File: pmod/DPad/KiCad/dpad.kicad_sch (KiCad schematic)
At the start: 13 parts, among them SW1 SW_Push, SW2 SW_Push, SW3 SW_Push, SW4 SW_Push

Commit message: Fixed resistor labels to correct format (10K).
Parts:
- R1, R2, R3, R4: value 10 k -> 10K
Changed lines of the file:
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@@
 			)
 		)
-		(property "Value" "10 k"
+		(property "Value" "10K"
 			(at 109.22 91.4399 0)
 			(effects
@@
 			)
 		)
-		(property "Value" "10 k"
+		(property "Value" "10K"
 			(at 81.28 91.4399 0)
 			(effects
@@
 			)
 		)
-		(property "Value" "10 k"
+		(property "Value" "10K"
 			(at 95.25 91.4399 0)
 			(effects
@@
 			)
 		)
-		(property "Value" "10 k"
+		(property "Value" "10K"
 			(at 123.19 91.4399 0)
 			(effects

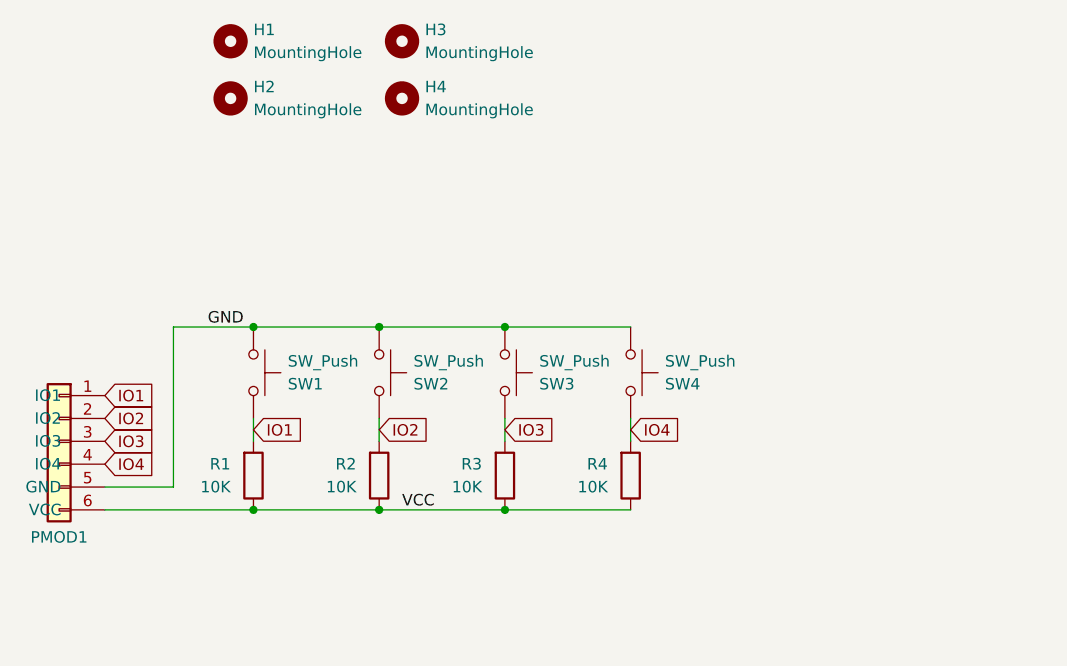
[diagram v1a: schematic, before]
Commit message: Added debounce capacitors. Added drill holes for switches.
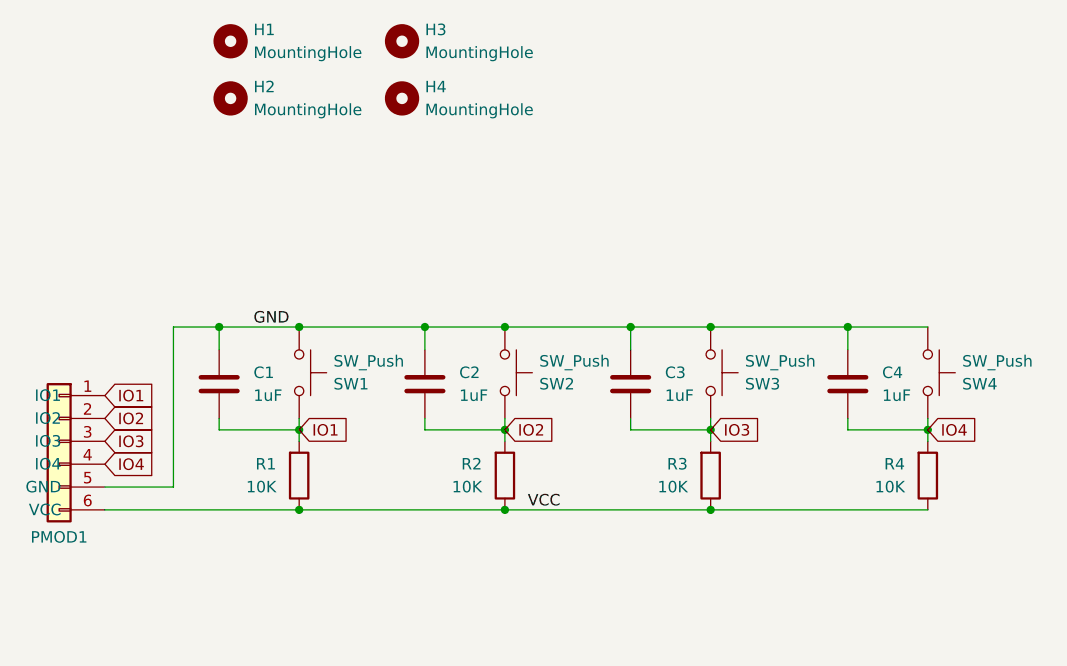
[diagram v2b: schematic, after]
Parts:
- added C1, C2, C3, C4: 1uF, Custom:C_Disc_D6.0mm_W4mm_P5.00mm, symbol Device:C
- SW1, SW2, SW3, SW4: footprint Button_Switch_THT:SW_PUSH-12mm_Wuerth-430476085716 -> Custom:SW_PUSH-12mm
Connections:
- net GND: now also C1.1, C2.1, C3.1, C4.1
- net IO1: now also C1.2
- net IO2: now also C2.2
- net IO3: now also C3.2
- net IO4: now also C4.2
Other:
- moved on the sheet: R1, R2, R3, R4, SW1, SW2, SW3, SW4

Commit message: Increased track width. Rounded edges of board. Fixed right angle connector.
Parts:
- PMOD1: footprint Connector_PinHeader_2.54mm:PinHeader_1x06_P2.54mm_Vertical -> Connector_PinHeader_2.54mm:PinHeader_1x06_P2.54mm_Horizontal
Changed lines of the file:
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@@
 			)
 		)
-		(property "Footprint" "Connector_PinHeader_2.54mm:PinHeader_1x06_P2.54mm_Vertical"
+		(property "Footprint" "Connector_PinHeader_2.54mm:PinHeader_1x06_P2.54mm_Horizontal"
 			(at 62.23 86.36 0)
 			(effects

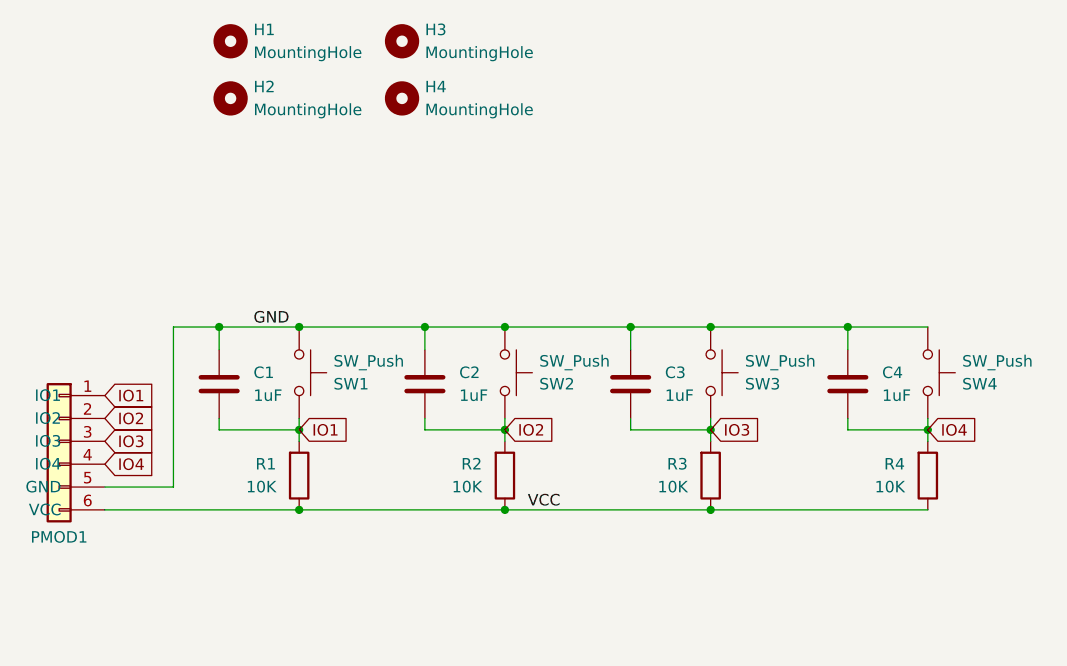
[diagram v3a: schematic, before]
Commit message: fix: prepare all board for manufacturing
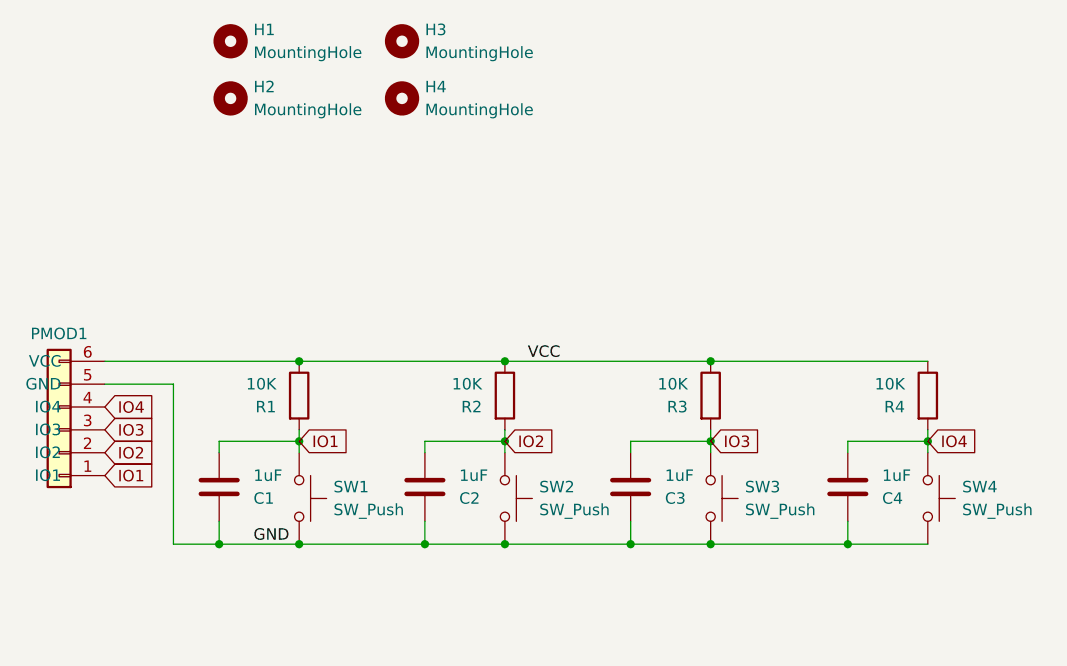
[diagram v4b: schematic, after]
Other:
- moved on the sheet: C1, C2, C3, C4, PMOD1, R1, R2, R3, R4, SW1, SW2, SW3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

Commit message: docs: add images, fix docs
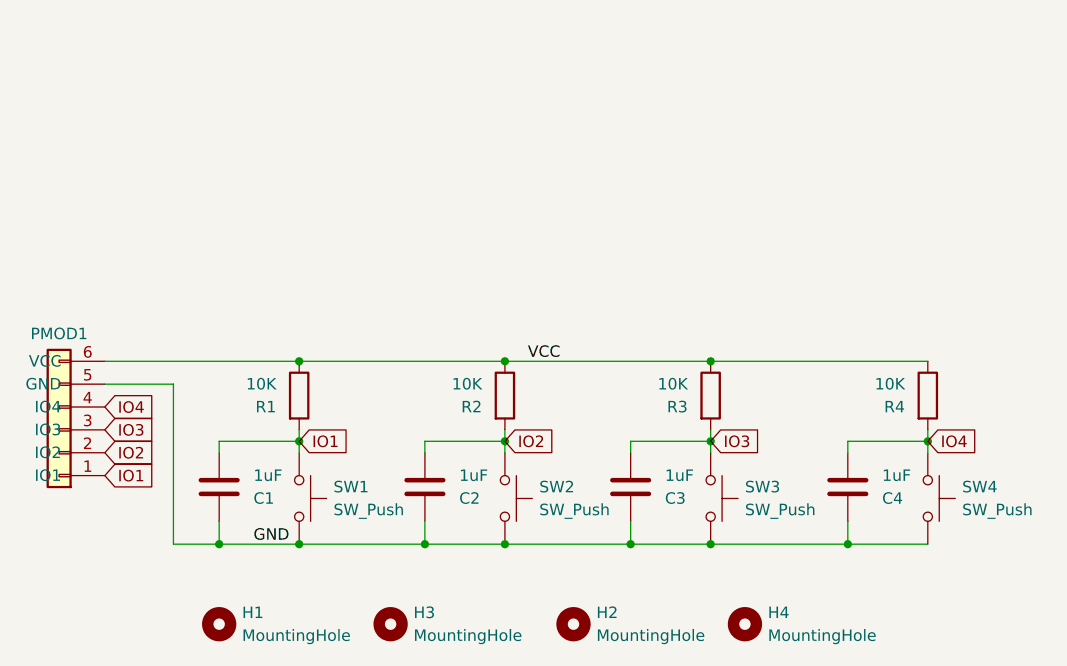
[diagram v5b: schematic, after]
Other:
- moved on the sheet: H1, H2, H3, H4
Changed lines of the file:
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@@
 	(symbol
 		(lib_id "Mechanical:MountingHole")
-		(at 81.28 48.26 0)
+		(at 119.38 106.68 0)
 		(unit 1)
 		(body_style 1)
@@
 		(fields_autoplaced yes)
 		(property "Reference" "H2"
-			(at 83.82 46.9899 0)
+			(at 121.92 105.4099 0)
 			(show_name no)
 			(do_not_autoplace no)
@@
 		)
 		(property "Value" "MountingHole"
-			(at 83.82 49.5299 0)
+			(at 121.92 107.9499 0)
 			(show_name no)
 			(do_not_autoplace no)
@@
 		)
 		(property "Footprint" "MountingHole:MountingHole_3.2mm_M3"
-			(at 81.28 48.26 0)
-			(hide yes)
-			(show_name no)
-			(do_not_autoplace no)
-			(effects
-				(font
-					(size 1.27 1.27)
-				)
-			)
-		)
-		(property "Datasheet" ""
-			(at 81.28 48.26 0)
+			(at 119.38 106.68 0)
+			(hide yes)
+			(show_name no)
+			(do_not_autoplace no)
+			(effects
+				(font
+					(size 1.27 1.27)
+				)
+			)
+		)
+		(property "Datasheet" ""
+			(at 119.38 106.68 0)
 			(hide yes)
 			(show_name no)
@@
 		)
 		(property "Description" "Mounting Hole without connection"
-			(at 81.28 48.26 0)
+			(at 119.38 106.68 0)
 			(hide yes)
 			(show_name no)
@@
 	(symbol
 		(lib_id "Mechanical:MountingHole")
-		(at 100.33 48.26 0)
+		(at 138.43 106.68 0)
 		(unit 1)
 		(body_style 1)
@@
 		(fields_autoplaced yes)
 		(property "Reference" "H4"
-			(at 102.87 46.9899 0)
+			(at 140.97 105.4099 0)
 			(show_name no)
 			(do_not_autoplace no)
@@
 		)
 		(property "Value" "MountingHole"
-			(at 102.87 49.5299 0)
+			(at 140.97 107.9499 0)
 			(show_name no)
 			(do_not_autoplace no)
@@
 		)
 		(property "Footprint" "MountingHole:MountingHole_3.2mm_M3"
-			(at 100.33 48.26 0)
-			(hide yes)
-			(show_name no)
-			(do_not_autoplace no)
-			(effects
-				(font
-					(size 1.27 1.27)
-				)
-			)
-		)
-		(property "Datasheet" ""
-			(at 100.33 48.26 0)
+			(at 138.43 106.68 0)
+			(hide yes)
+			(show_name no)
+			(do_not_autoplace no)
+			(effects
+				(font
+					(size 1.27 1.27)
+				)
+			)
+		)
+		(property "Datasheet" ""
+			(at 138.43 106.68 0)
 			(hide yes)
 			(show_name no)
@@
 		)
 		(property "Description" "Mounting Hole without connection"
-			(at 100.33 48.26 0)
+			(at 138.43 106.68 0)
 			(hide yes)
 			(show_name no)
@@
 	(symbol
 		(lib_id "Mechanical:MountingHole")
-		(at 100.33 41.91 0)
+		(at 99.06 106.68 0)
 		(unit 1)
 		(body_style 1)
@@
 		(fields_autoplaced yes)
 		(property "Reference" "H3"
-			(at 102.87 40.6399 0)
+			(at 101.6 105.4099 0)
 			(show_name no)
 			(do_not_autoplace no)
@@
 		)
 		(property "Value" "MountingHole"
-			(at 102.87 43.1799 0)
+			(at 101.6 107.9499 0)
 			(show_name no)
 			(do_not_autoplace no)
@@
 		)
 		(property "Footprint" "MountingHole:MountingHole_3.2mm_M3"
-			(at 100.33 41.91 0)
-			(hide yes)
-			(show_name no)
-			(do_not_autoplace no)
-			(effects
-				(font
-					(size 1.27 1.27)
-				)
-			)
-		)
-		(property "Datasheet" ""
-			(at 100.33 41.91 0)
+			(at 99.06 106.68 0)
+			(hide yes)
+			(show_name no)
+			(do_not_autoplace no)
+			(effects
+				(font
+					(size 1.27 1.27)
+				)
+			)
+		)
+		(property "Datasheet" ""
+			(at 99.06 106.68 0)
 			(hide yes)
 			(show_name no)
@@
 		)
 		(property "Description" "Mounting Hole without connection"
-			(at 100.33 41.91 0)
+			(at 99.06 106.68 0)
 			(hide yes)
 			(show_name no)
@@
 	(symbol
 		(lib_id "Mechanical:MountingHole")
-		(at 81.28 41.91 0)
+		(at 80.01 106.68 0)
 		(unit 1)
 		(body_style 1)
@@
 		(fields_autoplaced yes)
 		(property "Reference" "H1"
-			(at 83.82 40.6399 0)
+			(at 82.55 105.4099 0)
 			(show_name no)
 			(do_not_autoplace no)
@@
 		)
 		(property "Value" "MountingHole"
-			(at 83.82 43.1799 0)
+			(at 82.55 107.9499 0)
 			(show_name no)
 			(do_not_autoplace no)
@@
 		)
 		(property "Footprint" "MountingHole:MountingHole_3.2mm_M3"
-			(at 81.28 41.91 0)
-			(hide yes)
-			(show_name no)
-			(do_not_autoplace no)
-			(effects
-				(font
-					(size 1.27 1.27)
-				)
-			)
-		)
-		(property "Datasheet" ""
-			(at 81.28 41.91 0)
+			(at 80.01 106.68 0)
+			(hide yes)
+			(show_name no)
+			(do_not_autoplace no)
+			(effects
+				(font
+					(size 1.27 1.27)
+				)
+			)
+		)
+		(property "Datasheet" ""
+			(at 80.01 106.68 0)
 			(hide yes)
 			(show_name no)
@@
 		)
 		(property "Description" "Mounting Hole without connection"
-			(at 81.28 41.91 0)
-			(hide yes)
-			(show_name no)
+			(at 80.01 106.68 0)
+			(hide yes)
+			(show_name no)
